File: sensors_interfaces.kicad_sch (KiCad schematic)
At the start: 35 parts, among them IC1 PCF8563T_5,518, IC2 W25Q128JVSIQTR, IC5 SP3485EN-L_TR, IC8 STK8321, U1 TMP112xxDRL, X14 CH340G, X2 32.768 kHz, X3 TF-15×15, X4 CR1220-2ZX, Y1 X322512MSB4SI

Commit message: proceed with layout
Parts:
- added C25: 100nF, Capacitor_SMD:C_0402_1005Metric_Pad0.74x0.62mm_HandSolder, symbol eduboardv2:CL05B104KB54PNC
- added C26: 1uF, Capacitor_SMD:C_0402_1005Metric_Pad0.74x0.62mm_HandSolder, symbol eduboardv2:CL05A105KA5NQNC
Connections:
- net +3.3V: now also C25.2, C26.2
- net GND: now also C25.1, C26.1
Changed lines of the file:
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@@
   (junction (at 259.715 33.655) (diameter 0) (color 0 0 0 0)
   )
+  (junction (at 213.36 67.31) (diameter 0) (color 0 0 0 0)
+  )
   (junction (at 253.365 118.11) (diameter 0) (color 0 0 0 0)
   )
@@
   )
   (junction (at 263.525 38.735) (diameter 0) (color 0 0 0 0)
+  )
+  (junction (at 213.36 59.69) (diameter 0) (color 0 0 0 0)
   )
   (junction (at 88.265 50.165) (diameter 0) (color 0 0 0 0)
@@
     (stroke (width 0) (type default))
   )
+  (wire (pts (xy 203.835 67.31) (xy 213.36 67.31))
+    (stroke (width 0) (type default))
+  )
   (wire (pts (xy 194.945 22.225) (xy 199.39 22.225))
     (stroke (width 0) (type default))
@@
   )
   (wire (pts (xy 186.69 85.09) (xy 196.215 85.09))
+    (stroke (width 0) (type default))
+  )
+  (wire (pts (xy 203.835 59.69) (xy 213.36 59.69))
     (stroke (width 0) (type default))
   )
@@
     )
   )
+  (symbol (lib_id "eduboardv2:+3.3V") (at 213.36 59.69 0) (unit 1)
+    (in_bom yes) (on_board yes) (dnp no)
+    (property "Reference" "#PWR093" (at 213.36 63.5 0)
+      (effects (font (size 1.27 1.27)) hide)
+    )
+    (property "Value" "+3.3V" (at 213.36 53.34 90)
+      (effects (font (size 1.27 1.27)))
+    )
+    (property "Footprint" "" (at 213.36 59.69 0)
+      (effects (font (size 1.27 1.27)) hide)
+    )
+    (property "Datasheet" "" (at 213.36 59.69 0)
+      (effects (font (size 1.27 1.27)) hide)
+    )
+    (pin "1")
+    (instances
+      (project "EduboardV2_Baseboard"
+        (path "/280adf03-05ea-4001-ab24-a5a43e6d4cc9/92753037-c50f-47ac-9b4f-72ea899f1ef8"
+          (reference "#PWR093") (unit 1)
+        )
+        (path "/280adf03-05ea-4001-ab24-a5a43e6d4cc9/079bc49e-d545-405c-843f-4b3e915cef08"
+          (reference "#PWR0197") (unit 1)
+        )
+      )
+    )
+  )
   (symbol (lib_id "eduboardv2:GND") (at 113.665 60.325 270) (unit 1)
     (in_bom yes) (on_board yes) (dnp no)
@@
     )
   )
+  (symbol (lib_id "eduboardv2:GND") (at 213.36 67.31 0) (unit 1)
+    (in_bom yes) (on_board yes) (dnp no) (fields_autoplaced)
+    (property "Reference" "#PWR094" (at 213.36 73.66 0)
+      (effects (font (size 1.27 1.27)) hide)
+    )
+    (property "Value" "GND" (at 213.36 72.39 0)
+      (effects (font (size 1.27 1.27)))
+    )
+    (property "Footprint" "" (at 213.36 67.31 0)
+      (effects (font (size 1.27 1.27)) hide)
+    )
+    (property "Datasheet" "" (at 213.36 67.31 0)
+      (effects (font (size 1.27 1.27)) hide)
+    )
+    (pin "1")
+    (instances
+      (project "EduboardV2_Baseboard"
+        (path "/280adf03-05ea-4001-ab24-a5a43e6d4cc9/92753037-c50f-47ac-9b4f-72ea899f1ef8"
+          (reference "#PWR094") (unit 1)
+        )
+        (path "/280adf03-05ea-4001-ab24-a5a43e6d4cc9/079bc49e-d545-405c-843f-4b3e915cef08"
+          (reference "#PWR0198") (unit 1)
+        )
+      )
+    )
+  )
   (symbol (lib_id "eduboardv2:+3.3V") (at 194.945 20.32 0) (unit 1)
     (in_bom yes) (on_board yes) (dnp no)
@@
         (path "/280adf03-05ea-4001-ab24-a5a43e6d4cc9/079bc49e-d545-405c-843f-4b3e915cef08"
           (reference "JP8") (unit 1)
+        )
+      )
+    )
+  )
+  (symbol (lib_name "CL05B104KB54PNC_1") (lib_id "eduboardv2:CL05B104KB54PNC") (at 203.835 63.5 90) (unit 1)
+    (in_bom yes) (on_board yes) (dnp no)
+    (property "Reference" "C25" (at 204.47 61.595 90)
+      (effects (font (size 1.27 1.27)) (justify right))
+    )
+    (property "Value" "100nF" (at 204.47 66.04 90)
+      (effects (font (size 1.27 1.27)) (justify right))
+    )
+    (property "Footprint" "Capacitor_SMD:C_0402_1005Metric_Pad0.74x0.62mm_HandSolder" (at 211.455 63.5 0)
+      (effects (font (size 1.27 1.27)) hide)
+    )
+    (property "Datasheet" "https://lcsc.com/product-detail/Others_Samsung-Electro-Mechanics_CL05B104KB54PNC_Samsung-Electro-Mechanics-CL05B104KB54PNC_C307331.html" (at 216.535 63.5 0)
+      (effects (font (size 1.27 1.27)) hide)
+    )
+    (property "Manufacturer" "Samsung Electro-Mechanics" (at 219.075 63.5 0)
+      (effects (font (size 1.27 1.27)) hide)
+    )
+    (property "LCSC Part" "C307331" (at 221.615 63.5 0)
+      (effects (font (size 1.27 1.27)) hide)
+    )
+    (property "JLC Part" "Basic Part" (at 224.155 63.5 0)
+      (effects (font (size 1.27 1.27)) hide)
+    )
+    (property "MPN" "CL05B104KB54PNC" (at 208.915 63.5 0)
+      (effects (font (size 1.27 1.27)) hide)
+    )
+    (pin "1")
+    (pin "2")
+    (instances
+      (project "EduboardV2_Baseboard"
+        (path "/280adf03-05ea-4001-ab24-a5a43e6d4cc9/92753037-c50f-47ac-9b4f-72ea899f1ef8"
+          (reference "C25") (unit 1)
+        )
+        (path "/280adf03-05ea-4001-ab24-a5a43e6d4cc9/079bc49e-d545-405c-843f-4b3e915cef08"
+          (reference "C55") (unit 1)
         )
       )
@@
         )
       )
+    )
+  )
+  (symbol (lib_name "CL05A105KA5NQNC_1") (lib_id "eduboardv2:CL05A105KA5NQNC") (at 213.36 63.5 90) (unit 1)
+    (in_bom yes) (on_board yes) (dnp no)
+    (property "Reference" "C26" (at 213.995 61.595 90)
+      (effects (font (size 1.27 1.27)) (justify right))
+    )
+    (property "Value" "1uF" (at 213.995 66.04 90)
+      (effects (font (size 1.27 1.27)) (justify right))
+    )
+    (property "Footprint" "Capacitor_SMD:C_0402_1005Metric_Pad0.74x0.62mm_HandSolder" (at 220.98 63.5 0)
+      (effects (font (size 1.27 1.27)) hide)
+    )
+    (property "Datasheet" "https://lcsc.com/product-detail/Multilayer-Ceramic-Capacitors-MLCC-SMD-SMT_SAMSUNG_CL05A105KA5NQNC_1uF-105-10-25V_C52923.html" (at 226.06 63.5 0)
+      (effects (font (size 1.27 1.27)) hide)
+    )
+    (property "Manufacturer" "SAMSUNG" (at 228.6 63.5 0)
+      (effects (font (size 1.27 1.27)) hide)
+    )
+    (property "LCSC Part" "C52923" (at 231.14 63.5 0)
+      (effects (font (size 1.27 1.27)) hide)
+    )
+    (property "JLC Part" "Basic Part" (at 233.68 63.5 0)
+      (effects (font (size 1.27 1.27)) hide)
+    )
+    (property "MPN" "CL05A105KA5NQNC" (at 218.44 63.5 0)
+      (effects (font (size 1.27 1.27)) hide)
+    )
+    (pin "1")
+    (pin "2")
+    (instances
+      (project "EduboardV2_Baseboard"
+        (path "/280adf03-05ea-4001-ab24-a5a43e6d4cc9/92753037-c50f-47ac-9b4f-72ea899f1ef8"
+          (reference "C26") (unit 1)
+        )
+        (path "/280adf03-05ea-4001-ab24-a5a43e6d4cc9/079bc49e-d545-405c-843f-4b3e915cef08"
+          (reference "C56") (unit 1)
+        )
+      )

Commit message: work on layout.
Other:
- note added: "Address: 0x48 / 0x49"
- note added: "Address: 0x51 (W:0xA2/R:0xA3"
- note added: "Adress: 0x0F / 0x1F"
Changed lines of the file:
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@@
+    (effects (font (size 1.27 1.27)) (justify left bottom))
+  )
+  (text "Adress:\n0x0F / 0x1F" (at 202.565 21.59 0)
+    (effects (font (size 1.27 1.27)) (justify left bottom))
+  )
+  (text "Address:\n0x51 (W:0xA2/R:0xA3" (at 189.23 109.855 0)
+    (effects (font (size 1.27 1.27)) (justify left bottom))
+  )
+  (text "Address:\n0x48 / 0x49" (at 250.19 57.785 0)
     (effects (font (size 1.27 1.27)) (justify left bottom))
   )

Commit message: layout done so far. Have to check everything again
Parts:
- U1: JLC Part (none) -> Extended Part
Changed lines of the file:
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@@
+      (effects (font (size 1.27 1.27)) hide)
+    )
+    (property "JLC Part" "Extended Part" (at 269.875 70.485 0)
       (effects (font (size 1.27 1.27)) hide)
     )

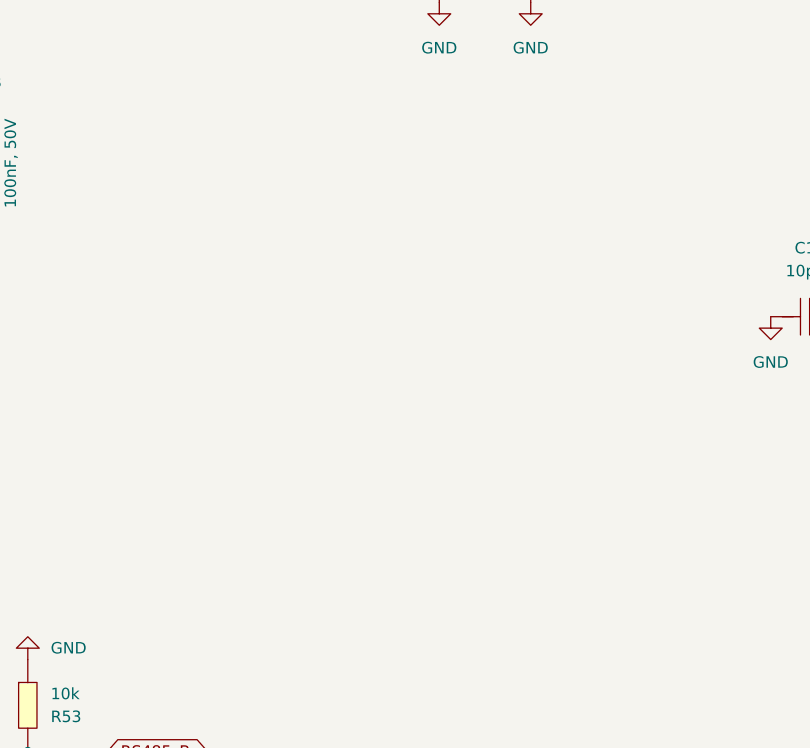
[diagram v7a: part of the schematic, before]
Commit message: add 2x DAC and fix I2C Impedance and Level Shifter
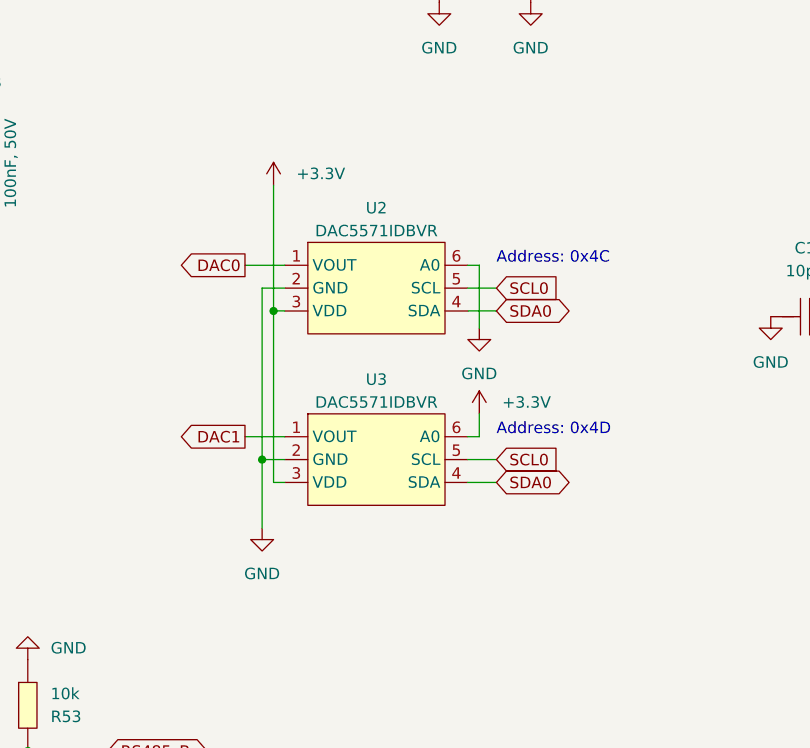
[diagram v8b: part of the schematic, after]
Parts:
- added U2, U3: DAC5571IDBVR, EduboardV2_kicadlib:SOT-23-6_L2.9-W1.6-P0.95-LS2.8-BR, symbol EduboardV2_kicadlib:DAC5571IDBVR
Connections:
- net +3.3V: now also U2.3 (VDD), U3.3 (VDD), U3.6 (A0)
- net GND: now also U2.2 (GND), U2.6 (A0), U3.2 (GND)
- net SCL0: now also U2.5 (SCL), U3.5 (SCL)
- net SDA0: now also U2.4 (SDA), U3.4 (SDA)
- new net DAC0: U2.1 (VOUT)
- new net DAC1: U3.1 (VOUT)
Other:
- note added: "Address: 0x4C"
- note added: "Address: 0x4D"
